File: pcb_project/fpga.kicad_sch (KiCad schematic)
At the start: 38 parts, among them J7 FTSH-107-01-F-DV-K, U1 XC7A100T-FTG256

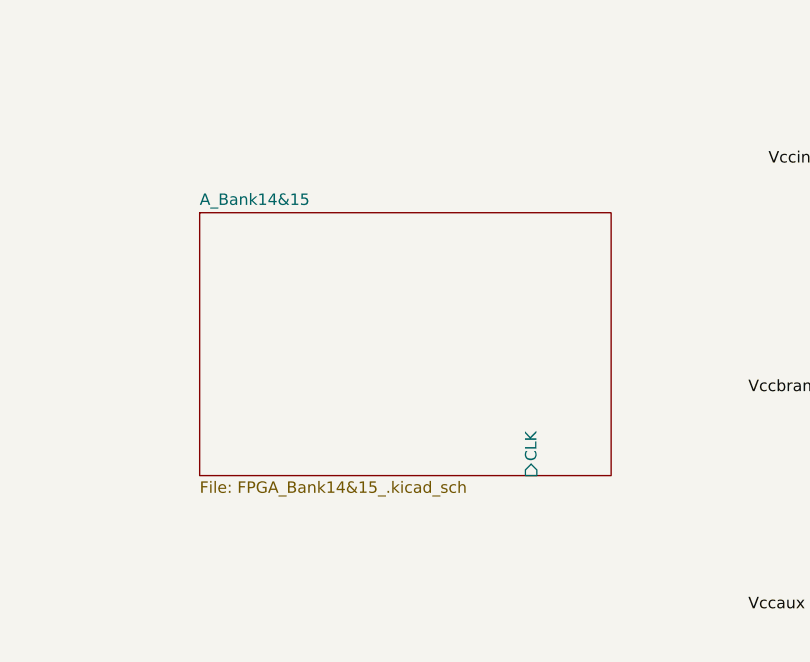
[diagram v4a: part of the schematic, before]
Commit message: Add pin placement for OSPI on FPGA, not wired in root yet
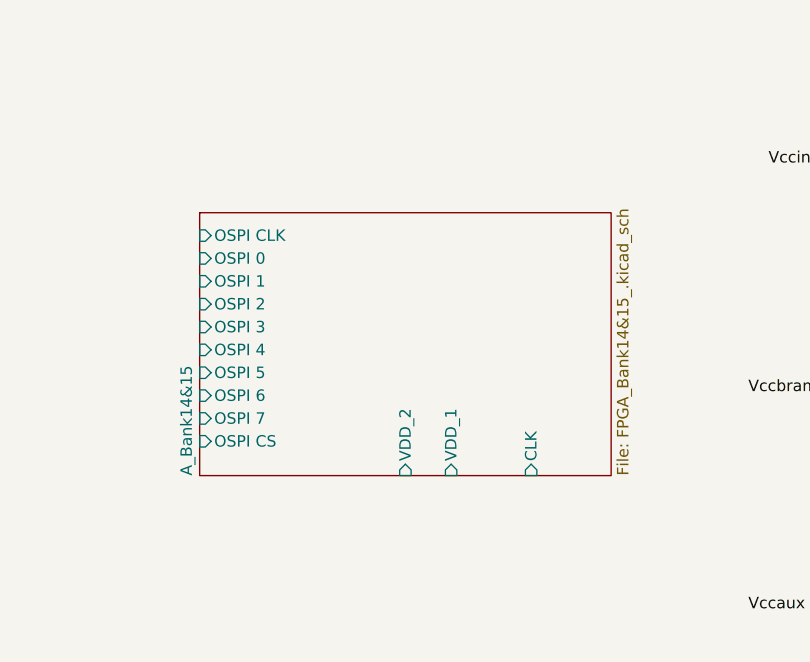
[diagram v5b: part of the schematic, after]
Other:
- sheet A_Bank14&15 ports: added OSPI 0, OSPI 1, OSPI 2, OSPI 3, OSPI 4, OSPI 5, OSPI 6, OSPI 7, OSPI CLK, OSPI CS, VDD_1, VDD_2; removed none
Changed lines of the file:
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@@
 		)
 		(property "Sheetname" "A_Bank14&15"
-			(at 29.21 34.8484 0)
+			(at 28.4984 64.77 90)
 			(effects
 				(font
@@
 		)
 		(property "Sheetfile" "FPGA_Bank14&15_.kicad_sch"
-			(at 29.21 65.3546 0)
+			(at 75.5146 64.77 90)
 			(effects
 				(font
@@
 			(effects
 				(font
+					(size 1.27 1.27)
+				)
+				(justify left)
+			)
+		)
+		(pin "OSPI CLK" input
+			(at 29.21 38.1 180)
+			(effects
+				(font
+					(size 1.27 1.27)
+				)
+				(justify left)
+			)
+		)
+		(pin "OSPI 1" input
+			(at 29.21 43.18 180)
+			(effects
+				(font
+					(size 1.27 1.27)
+				)
+				(justify left)
+			)
+		)
+		(pin "VDD_2" input
+			(at 52.07 64.77 270)
+			(effects
+				(font
+					(size 1.27 1.27)
+				)
+				(justify left)
+			)
+		)
+		(pin "VDD_1" input
+			(at 57.15 64.77 270)
+			(effects
+				(font
+					(size 1.27 1.27)
+				)
+				(justify left)
+			)
+		)
+		(pin "OSPI 6" input
+			(at 29.21 55.88 180)
+			(effects
+				(font
+					(size 1.27 1.27)
+				)
+				(justify left)
+			)
+		)
+		(pin "OSPI CS" input
+			(at 29.21 60.96 180)
+			(effects
+				(font
+					(size 1.27 1.27)
+				)
+				(justify left)
+			)
+		)
+		(pin "OSPI 2" input
+			(at 29.21 45.72 180)
+			(effects
+				(font
+					(size 1.27 1.27)
+				)
+				(justify left)
+			)
+		)
+		(pin "OSPI 0" input
+			(at 29.21 40.64 180)
+			(effects
+				(font
+					(size 1.27 1.27)
+				)
+				(justify left)
+			)
+		)
+		(pin "OSPI 5" input
+			(at 29.21 53.34 180)
+			(effects
+				(font
+					(size 1.27 1.27)
+				)
+				(justify left)
+			)
+		)
+		(pin "OSPI 3" input
+			(at 29.21 48.26 180)
+			(effects
+				(font
+					(size 1.27 1.27)
+				)
+				(justify left)
+			)
+		)
+		(pin "OSPI 4" input
+			(at 29.21 50.8 180)
+			(effects
+				(font
+					(size 1.27 1.27)
+				)
+				(justify left)
+			)
+		)
+		(pin "OSPI 7" input
+			(at 29.21 58.42 180)
+			(effects
+				(font

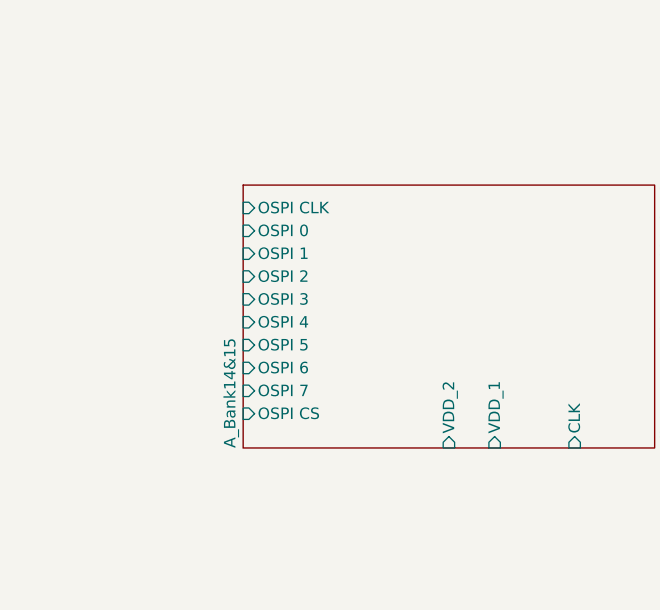
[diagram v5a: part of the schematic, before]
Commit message: SPI connection root
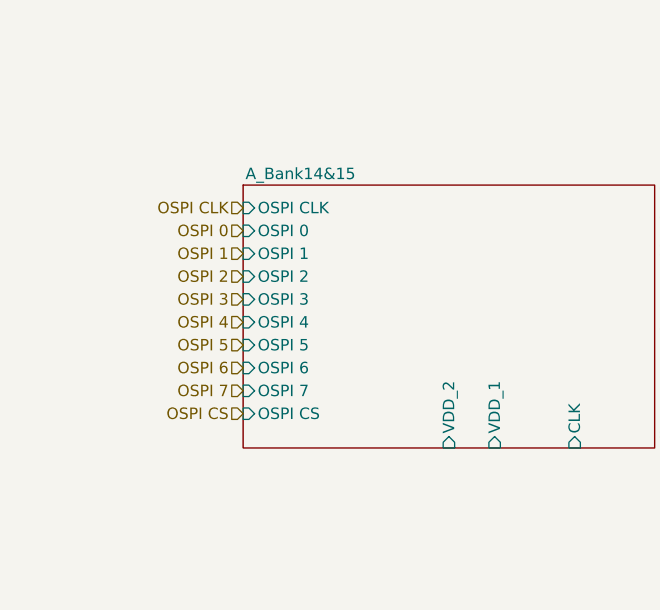
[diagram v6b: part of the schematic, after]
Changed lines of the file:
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@@
 		)
 	)
+	(hierarchical_label "OSPI CS"
+		(shape input)
+		(at 29.21 60.96 180)
+		(effects
+			(font
+				(size 1.27 1.27)
+			)
+			(justify right)
+		)
+	)
+	(hierarchical_label "OSPI 1"
+		(shape input)
+		(at 29.21 43.18 180)
+		(effects
+			(font
+				(size 1.27 1.27)
+			)
+			(justify right)
+		)
+	)
+	(hierarchical_label "OSPI 6"
+		(shape input)
+		(at 29.21 55.88 180)
+		(effects
+			(font
+				(size 1.27 1.27)
+			)
+			(justify right)
+		)
+	)
 	(hierarchical_label "VccAux"
 		(shape input)
@@
 		)
 	)
+	(hierarchical_label "OSPI 5"
+		(shape input)
+		(at 29.21 53.34 180)
+		(effects
+			(font
+				(size 1.27 1.27)
+			)
+			(justify right)
+		)
+	)
+	(hierarchical_label "OSPI CLK"
+		(shape input)
+		(at 29.21 38.1 180)
+		(effects
+			(font
+				(size 1.27 1.27)
+			)
+			(justify right)
+		)
+	)
 	(hierarchical_label "Vcco_0"
 		(shape input)
@@
 		)
 	)
+	(hierarchical_label "OSPI 2"
+		(shape input)
+		(at 29.21 45.72 180)
+		(effects
+			(font
+				(size 1.27 1.27)
+			)
+			(justify right)
+		)
+	)
+	(hierarchical_label "OSPI 4"
+		(shape input)
+		(at 29.21 50.8 180)
+		(effects
+			(font
+				(size 1.27 1.27)
+			)
+			(justify right)
+		)
+	)
+	(hierarchical_label "OSPI 7"
+		(shape input)
+		(at 29.21 58.42 180)
+		(effects
+			(font
+				(size 1.27 1.27)
+			)
+			(justify right)
+		)
+	)
+	(hierarchical_label "OSPI 3"
+		(shape input)
+		(at 29.21 48.26 180)
+		(effects
+			(font
+				(size 1.27 1.27)
+			)
+			(justify right)
+		)
+	)
+	(hierarchical_label "OSPI 0"
+		(shape input)
+		(at 29.21 40.64 180)
+		(effects
+			(font
+				(size 1.27 1.27)
+			)
+			(justify right)
+		)
+	)
 	(hierarchical_label "CLK"
 		(shape output)
@@
 		(on_board yes)
 		(dnp no)
-		(fields_autoplaced yes)
 		(stroke
 			(width 0.1524)
@@
 		)
 		(property "Sheetname" "A_Bank14&15"
-			(at 28.4984 64.77 90)
+			(at 29.464 35.052 0)
 			(effects
 				(font

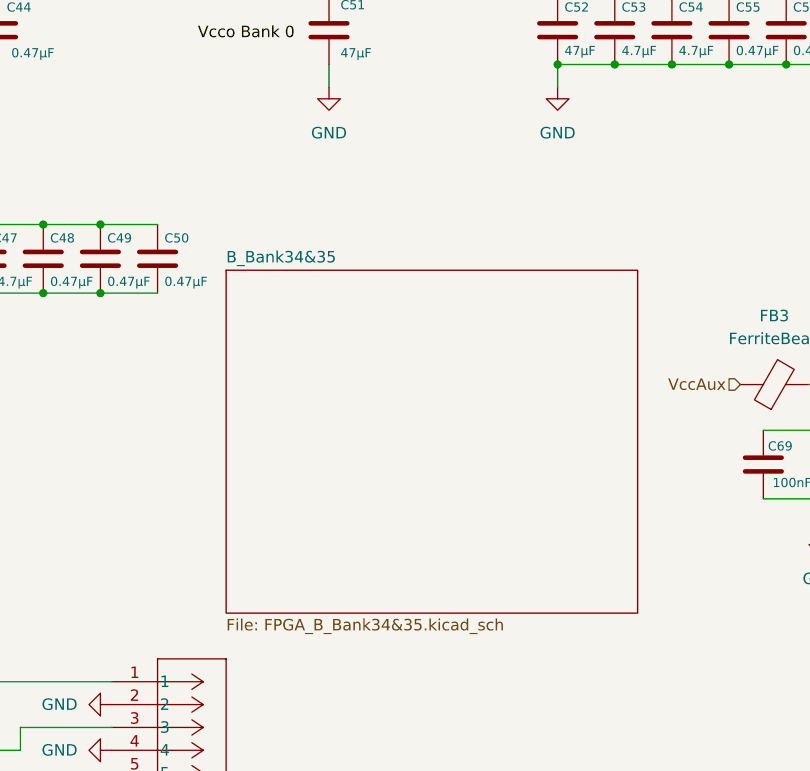
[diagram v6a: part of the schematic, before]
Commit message: VGA Root + Change FPGA Oscilator to 3.3v
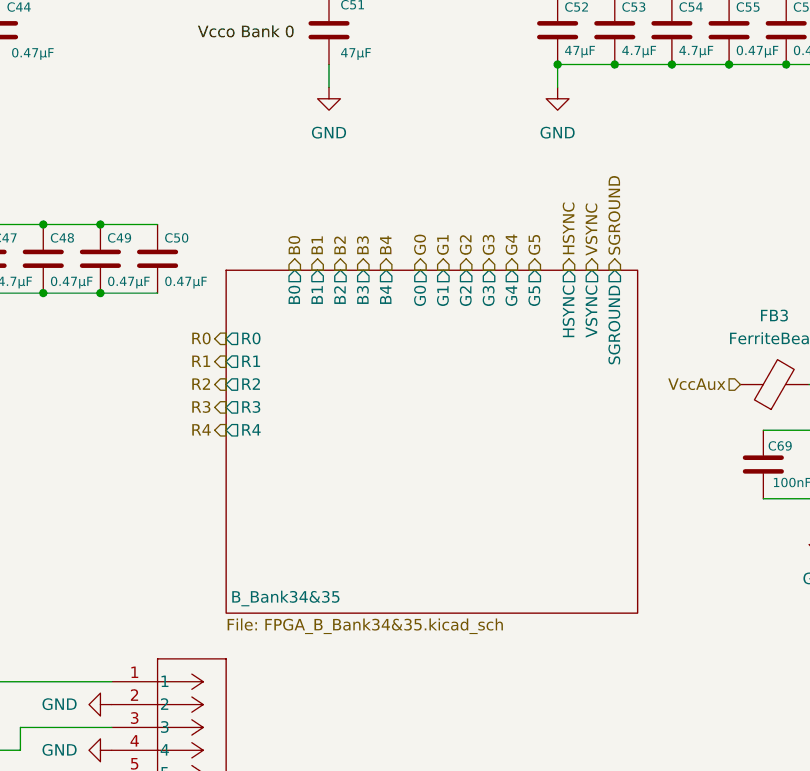
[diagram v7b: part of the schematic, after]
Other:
- sheet B_Bank34&35 ports: added B0, B1, B2, B3, B4, G0, G1, G2, G3, G4, G5, HSYNC, R0, R1, R2, R3, R4, SGROUND, VSYNC; removed none

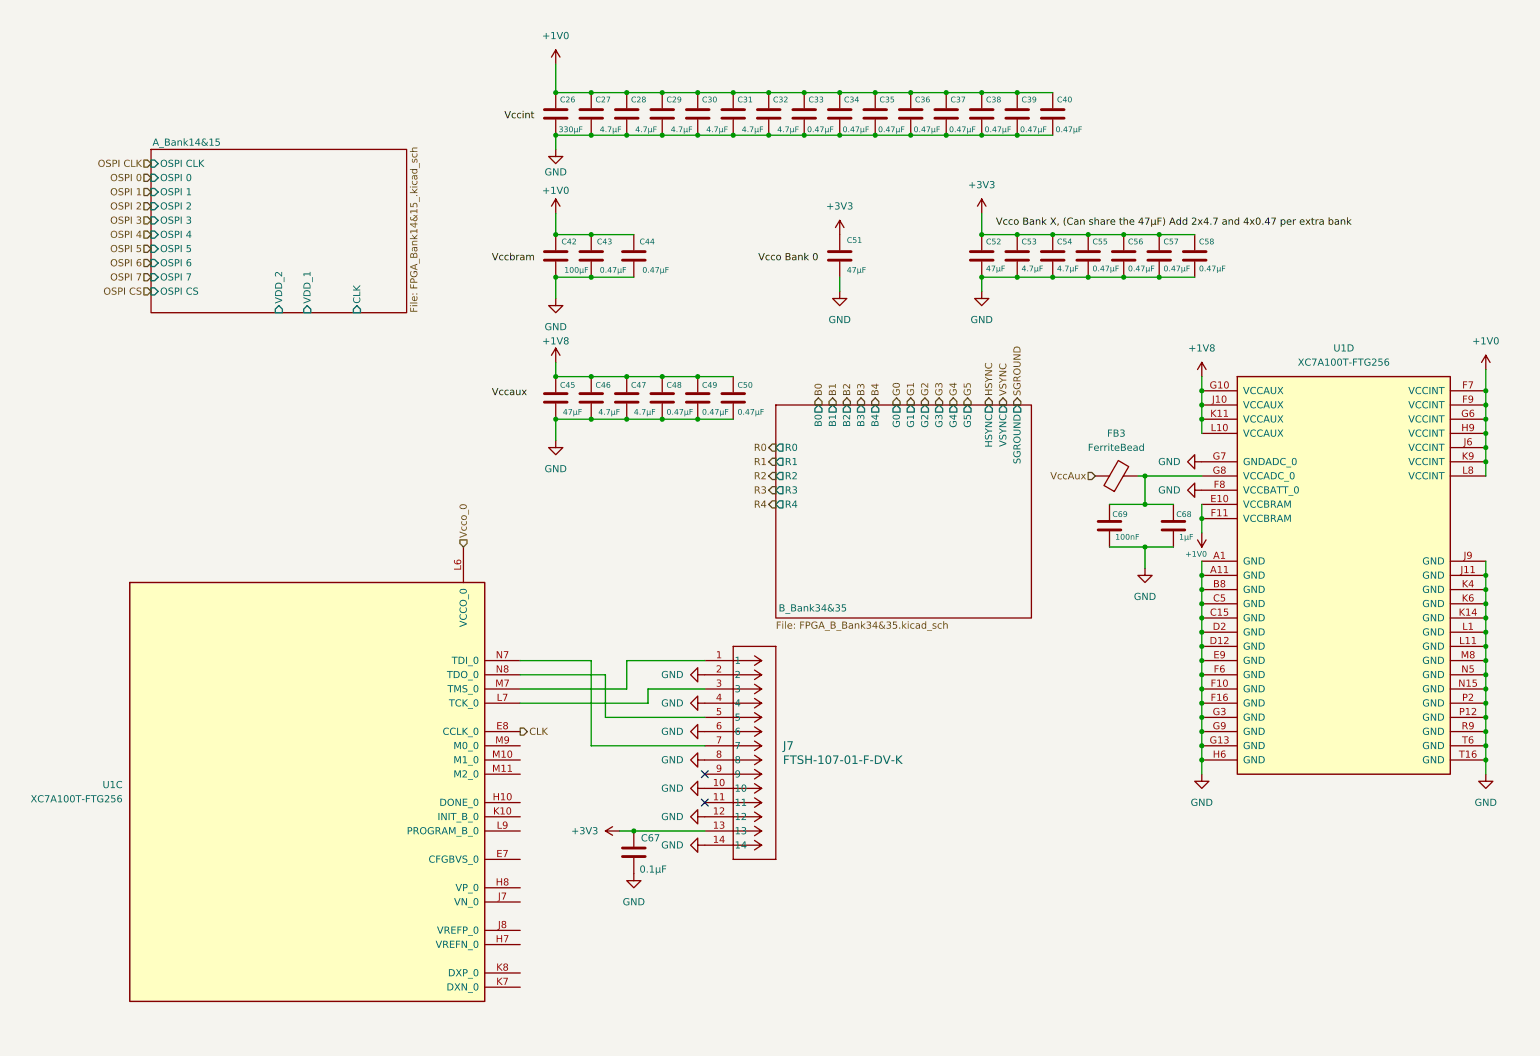
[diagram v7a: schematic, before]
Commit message: Add FPGA configuration LED's, config pins, no connect symbols
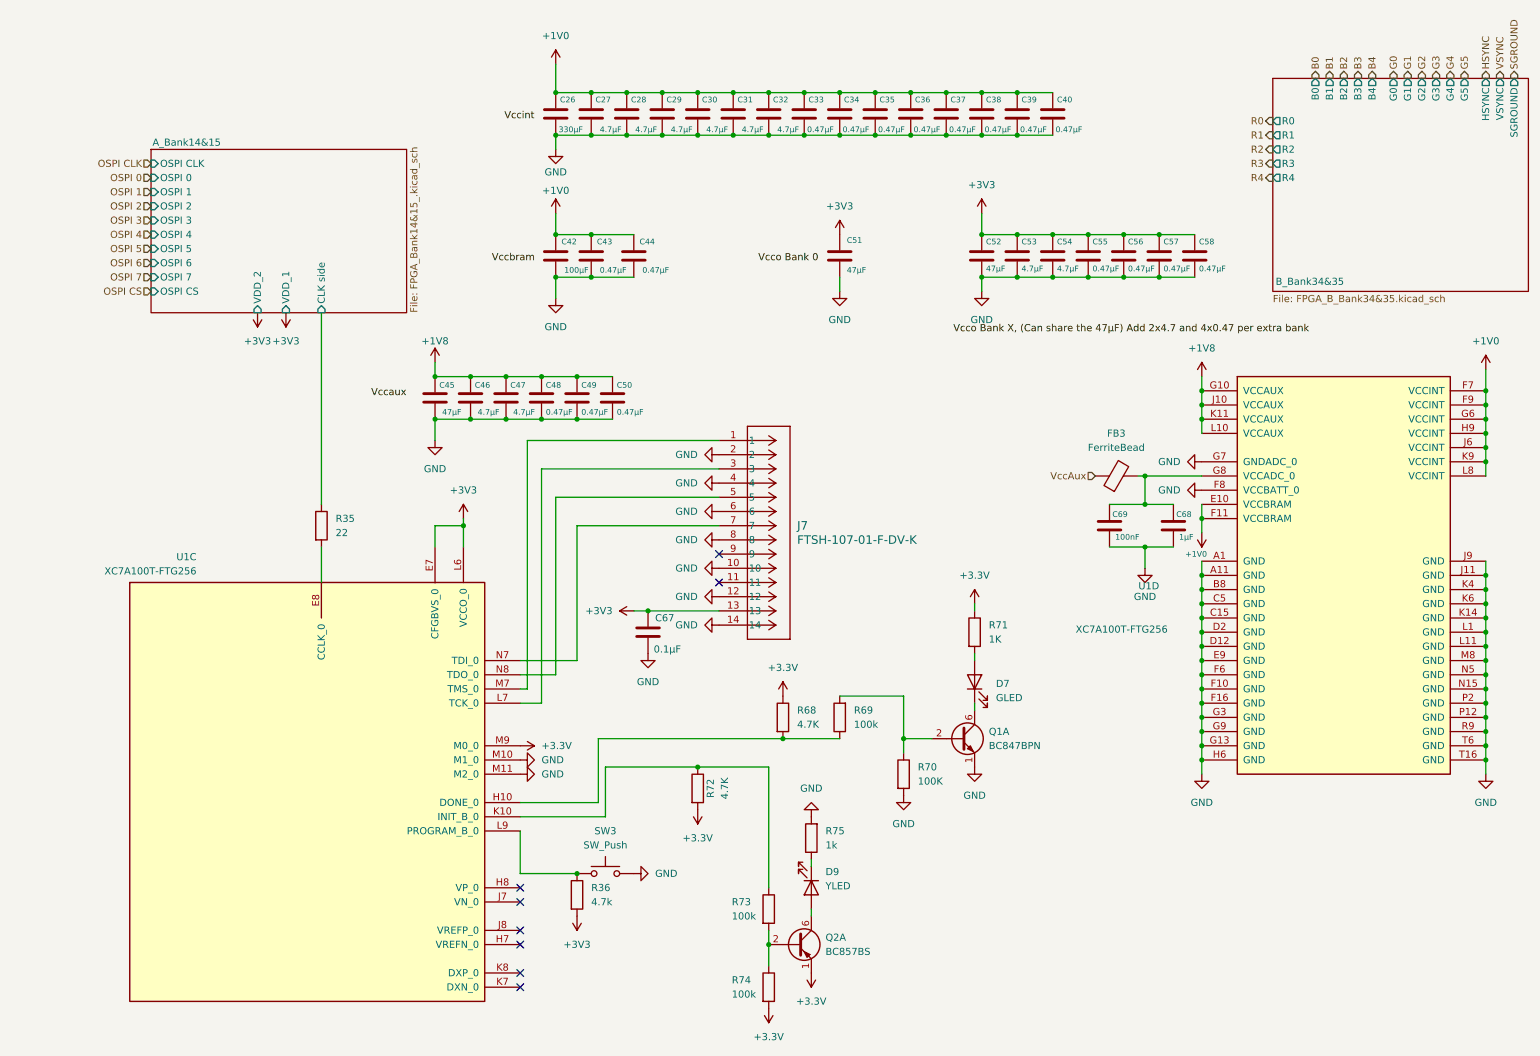
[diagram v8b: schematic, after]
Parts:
- added D7: GLED, symbol Device:LED
- added D9: YLED, symbol Device:LED
- added Q1: BC847BPN, Package_TO_SOT_SMD:SOT-363_SC-70-6, symbol Transistor_BJT:BC847BPN
- added Q2: BC857BS, Package_TO_SOT_SMD:SOT-363_SC-70-6, symbol Transistor_BJT:BC857BS
- added R35: 22, symbol Device:R
- added R36: 4.7k, symbol Device:R
- added R68, R72: 4.7K, symbol Device:R
- added R69, R73, R74: 100k, symbol Device:R
- added R70: 100K, symbol Device:R
- added R71: 1K, symbol Device:R
- added R75: 1k, symbol Device:R
- added SW3: SW_Push, symbol Switch:SW_Push
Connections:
- net Vcco_0 is gone; now on net +3V3: U1.L6 (VCCO_0)
- net +3V3: now also R36.2
- net GND: now also U1.M10 (M1_0), U1.M11 (M2_0), Q1.1 (E1), R70.2, R75.2, SW3.2
- net at U1.H10 (DONE_0): now also R68.2, R69.1
- net at U1.K10 (INIT_B_0): now also R72.1, R73.1
- net at U1.L9 (PROGRAM_B_0): now also R36.1, SW3.1
- net +3.3V: now reaches U1.M9 (M0_0)
- net +3.3V: now also Q2.1 (E1), R68.1, R71.1, R72.2, R74.2
- net CLK: no longer names the net of U1.E8 (CCLK_0)
- net CLK: now also R35.2
- new net: D9.1 (K), R75.1
- new net: D9.2 (A), Q2.6 (C1)
- new net: Q1.2 (B1), R69.2, R70.1
- new net: D7.2 (A), R71.2
- new net: D7.1 (K), Q1.6 (C1)
- new net: Q2.2 (B1), R73.2, R74.1
- new net A_Bank14&15/CLK side: R35.1
- no-connect marks 2 -> 8
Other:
- sheet A_Bank14&15 ports: added CLK side; removed CLK
- moved on the sheet: C45, C46, C47, C48, C49, C50, C67, J7
